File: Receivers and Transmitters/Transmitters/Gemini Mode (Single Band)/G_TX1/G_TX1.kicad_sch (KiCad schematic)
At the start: 15 parts, among them J1 Conn_01x05_Socket, J2 Conn_01x03_Socket, J3 Conn_01x04_Socket, J4 Conn_02x06_Odd_Even, U1 TPS7A4701xRGW, U2 ESP32-WROOM-32, U3 E28-2G4M27S, U5 E28-2G4M27S

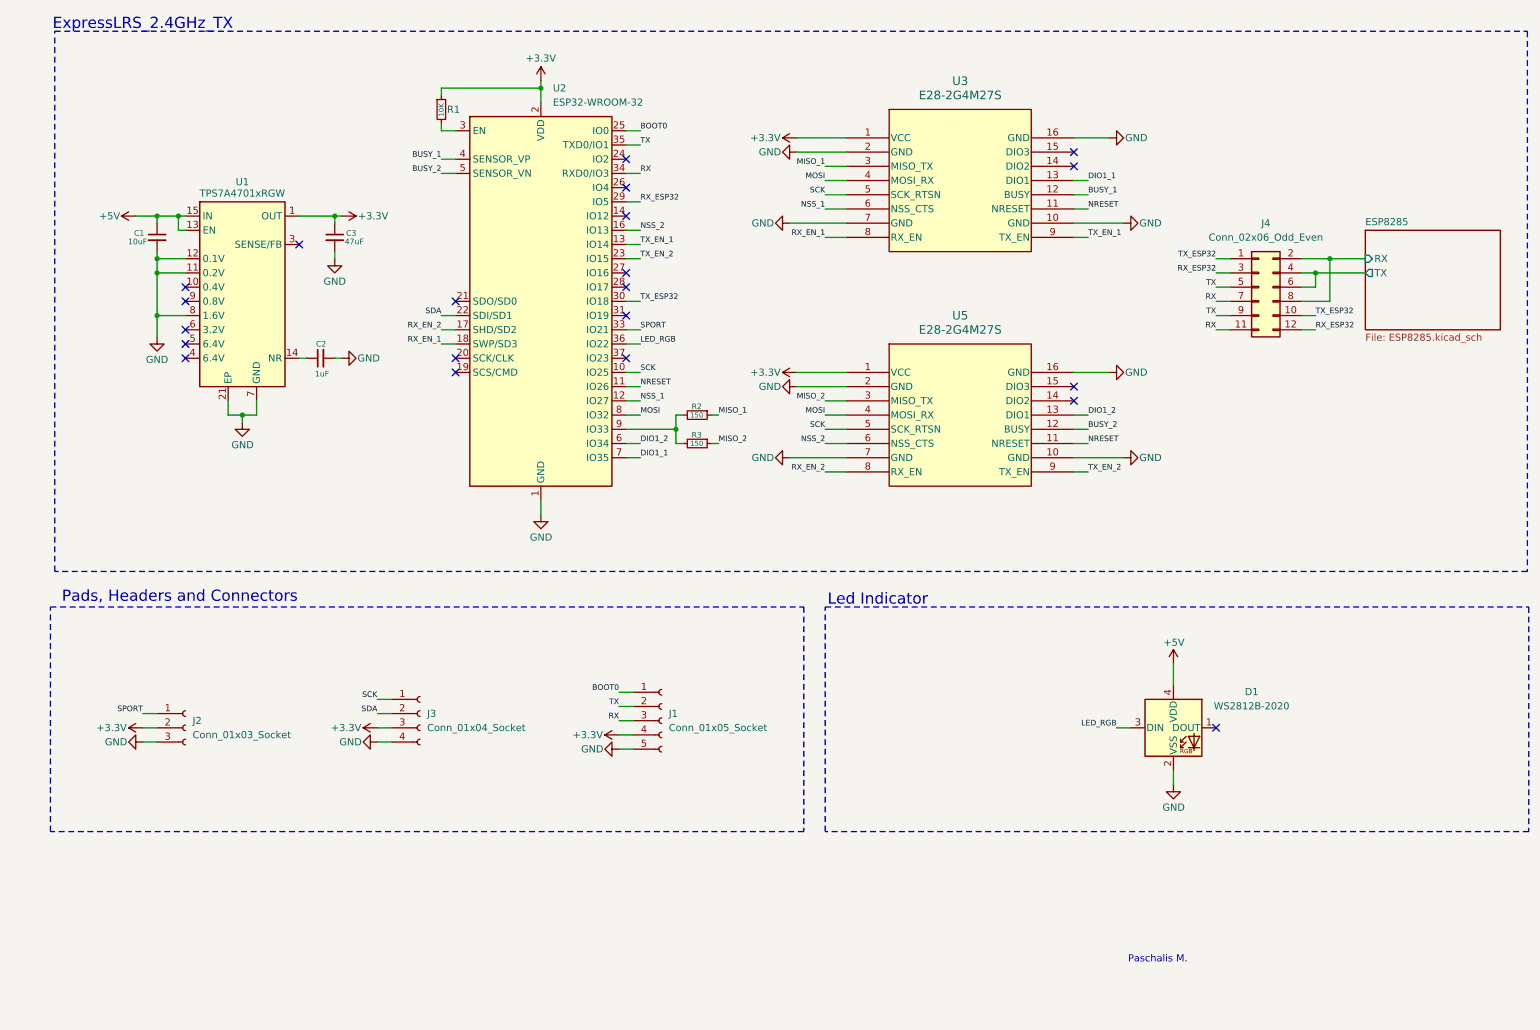
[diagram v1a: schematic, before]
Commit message: Update Antenna Diversity (AD1_2.4G), True Antenna Diversity (TD1_2.4G), and Gemini Mode transmitter (G_TX1): Modify KiCad files, add BOMs and production files; update images, docs, videos, and README; remove outdated Mechanical CAD file
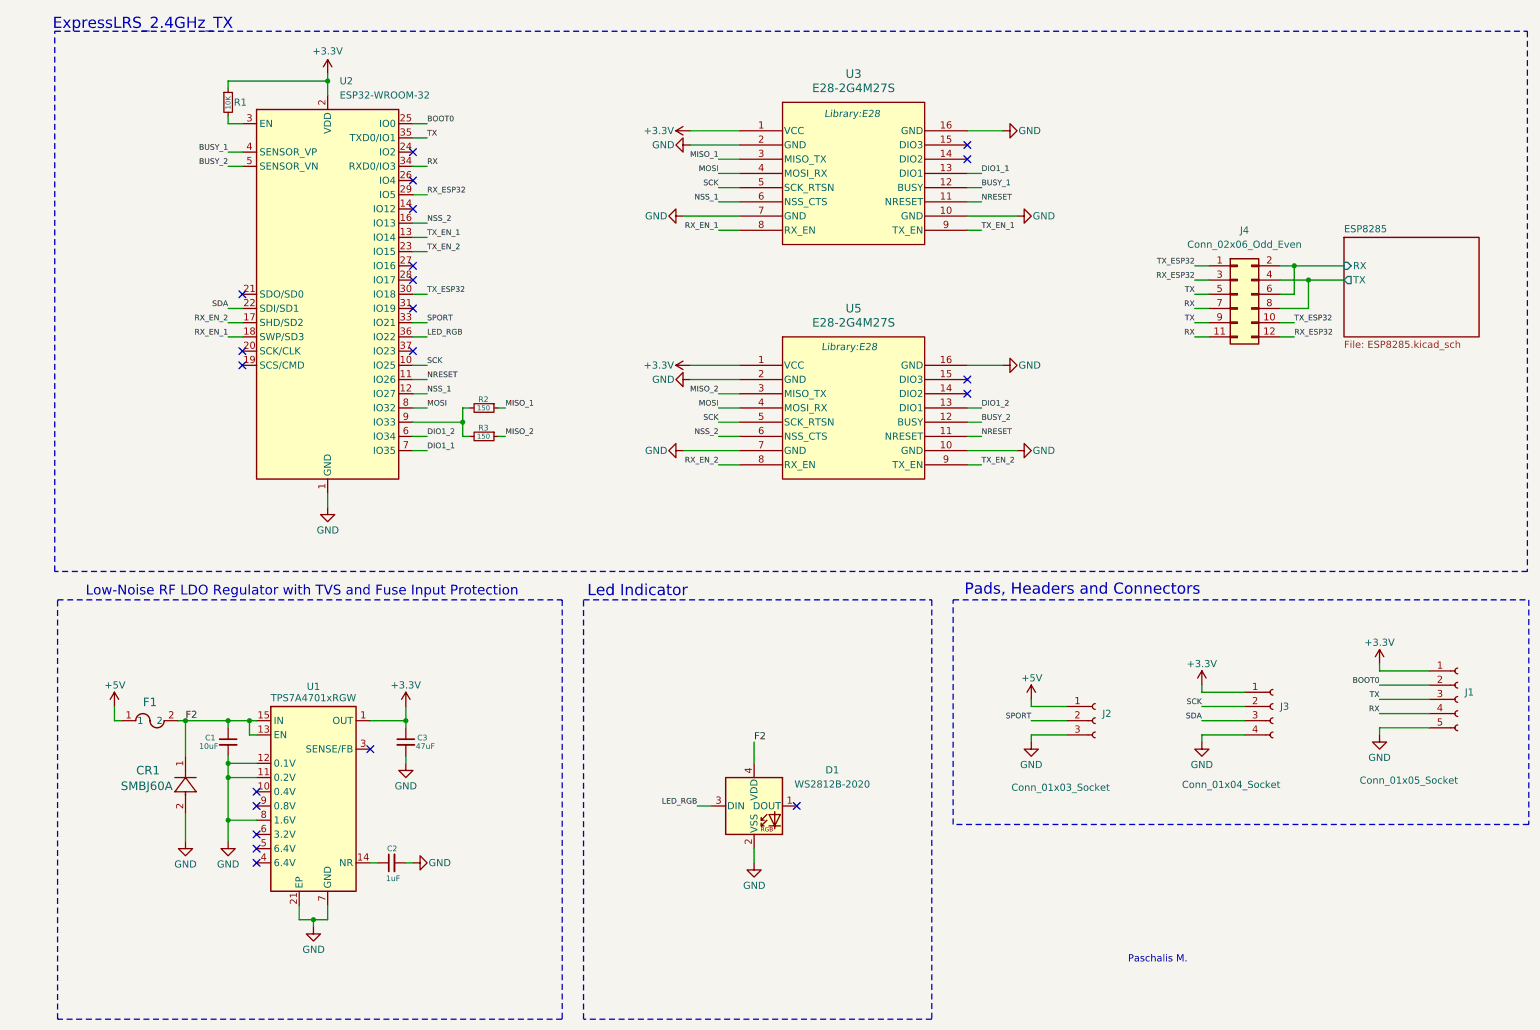
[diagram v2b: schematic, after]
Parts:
- added CR1: SMBJ60A, ul_SMBJ60A:SMBJSeries_LTF, symbol ul_SMBJ60A:SMBJ60A
- added F1: MF-PSMF020X-2, ul_MF-PSMF020X-2:FUSE_F020X_BRN, symbol ul_MF-PSMF020X-2:MF-PSMF020X-2
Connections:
- net +3.3V: now also J1.1 (Pin_1), J3.1 (Pin_1); no longer J1.4 (Pin_4), J2.2 (Pin_2), J3.3 (Pin_3)
- net +5V: now also J2.1 (Pin_1), F1.1; no longer C1.1, D1.4 (VDD), U1.13 (EN), U1.15 (IN), U1.16 (IN)
- net BOOT0: now also J1.2 (Pin_2); no longer J1.1 (Pin_1)
- net ESP8285/RX: now also J4.6 (Pin_6); no longer J4.8 (Pin_8)
- net ESP8285/TX: now also J4.8 (Pin_8); no longer J4.6 (Pin_6)
- net GND: now also CR1.2
- net RX: now also J1.4 (Pin_4); no longer J1.3 (Pin_3)
- net SCK: now also J3.2 (Pin_2); no longer J3.1 (Pin_1)
- net SDA: now also J3.3 (Pin_3); no longer J3.2 (Pin_2)
- net SPORT: now also J2.2 (Pin_2); no longer J2.1 (Pin_1)
- net TX: now also J1.3 (Pin_3); no longer J1.2 (Pin_2)
- new net F2: C1.1, CR1.1, D1.4 (VDD), F1.2, U1.13 (EN), U1.15 (IN), U1.16 (IN)
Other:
- note added: "Low-Noise RF LDO Regulator with TVS and Fuse Input Protection"
- company: https://github.com/Paschalis | TeodoraMiu -> https://github.com/Paschalis
- title: TX3_2.4G -> G_TX1_2.4G
- moved on the sheet: C1, C2, C3, D1, J1, J2, J3, J4, R1, R2, R3, U1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

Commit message: Update G_TX1 Freecad for enclosure and KiCad files (schematics, PCB, and project) - added fan pin headers
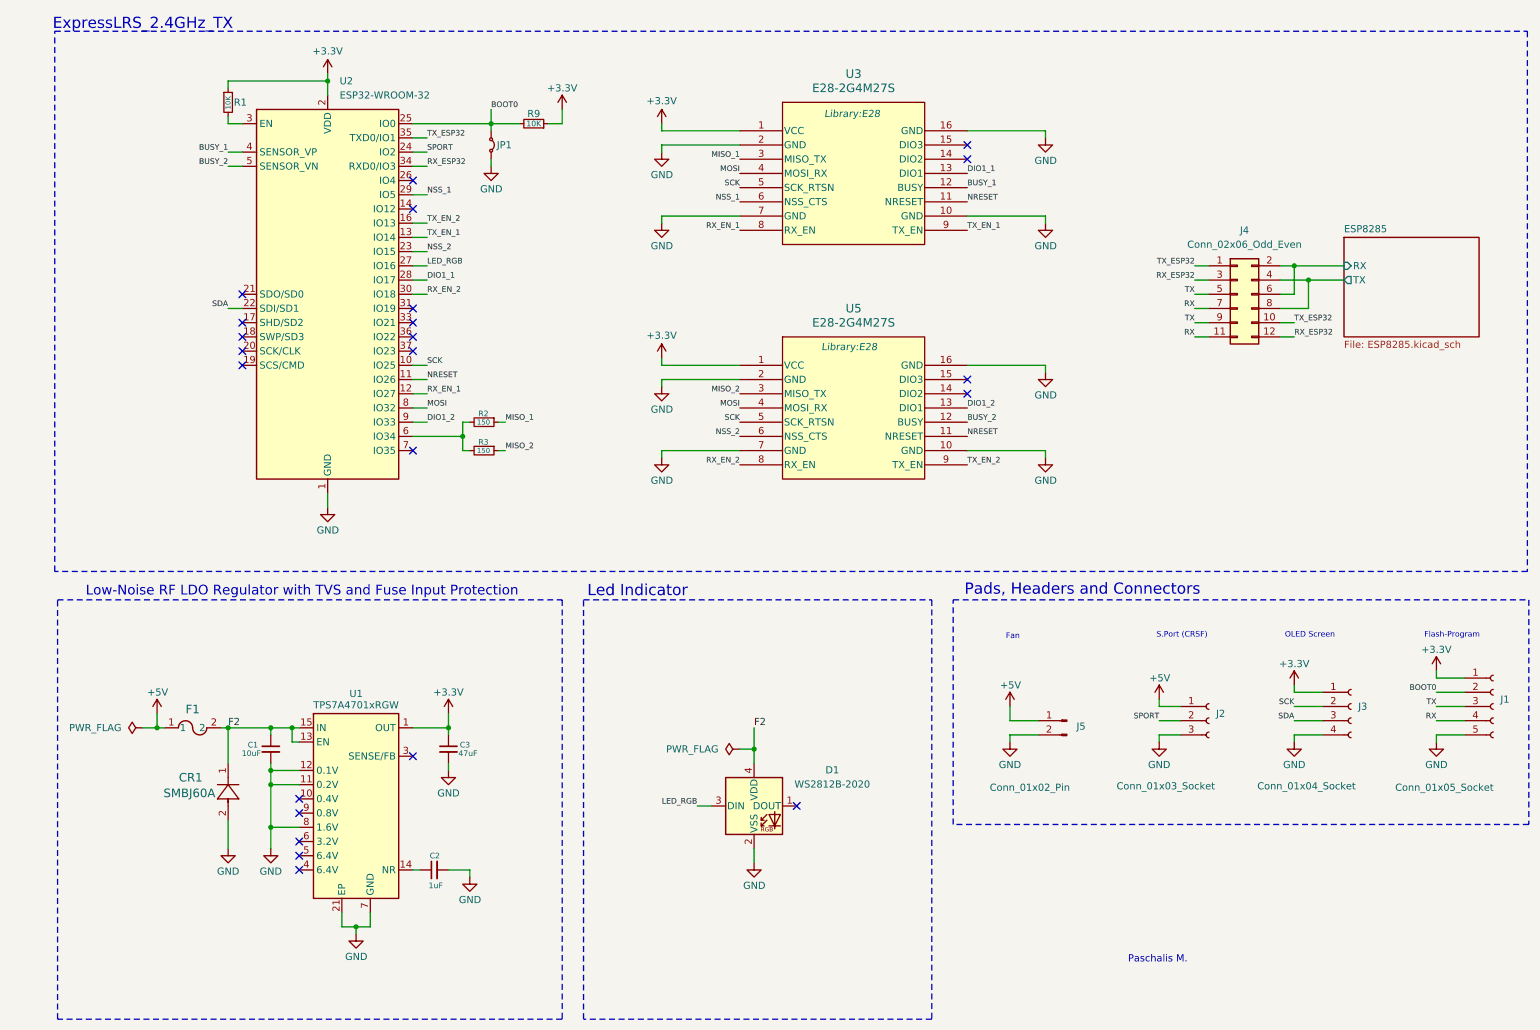
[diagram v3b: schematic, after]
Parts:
- added J5: Conn_01x02_Pin, Connector_PinHeader_2.00mm:PinHeader_1x02_P2.00mm_Vertical, symbol Connector:Conn_01x02_Pin
- added JP1: Jumper_2_Small_Bridged, TestPoint:TestPoint_2Pads_Pitch2.54mm_Drill0.8mm, symbol Jumper:Jumper_2_Small_Bridged
- added R9: 10K, Resistor_SMD:R_0603_1608Metric_Pad0.98x0.95mm_HandSolder, symbol Device:R_Small
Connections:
- net +3.3V: now also R9.1
- net +5V: now also J5.1 (Pin_1)
- net BOOT0: now also JP1.1 (A), R9.2
- net DIO1_1: now also U2.28 (IO17); no longer U2.7 (IO35)
- net DIO1_2: now also U2.9 (IO33); no longer U2.6 (IO34)
- net GND: now also J5.2 (Pin_2), JP1.2 (B)
- net LED_RGB: now also U2.27 (IO16); no longer U2.36 (IO22)
- net NSS_1: now also U2.29 (IO5); no longer U2.12 (IO27)
- net NSS_2: now also U2.23 (IO15); no longer U2.16 (IO13)
- net RX: no longer U2.34 (RXD0/IO3)
- net RX_EN_1: now also U2.12 (IO27); no longer U2.18 (SWP/SD3)
- net RX_EN_2: now also U2.30 (IO18); no longer U2.17 (SHD/SD2)
- net RX_ESP32: now also U2.34 (RXD0/IO3); no longer U2.29 (IO5)
- net SPORT: now also U2.24 (IO2); no longer U2.33 (IO21)
- net TX: no longer U2.35 (TXD0/IO1)
- net TX_EN_2: now also U2.16 (IO13); no longer U2.23 (IO15)
- net TX_ESP32: now also U2.35 (TXD0/IO1); no longer U2.30 (IO18)
- net at R2.2, R3.2: now also U2.6 (IO34); no longer U2.9 (IO33)
- no-connect marks 21 -> 23
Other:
- note added: "Fan"
- note added: "Flash-Program"
- note added: "OLED Screen"
- note added: "S.Port (CRSF)"
- moved on the sheet: C1, C2, C3, CR1, F1, J1, J2, J3, R2, R3, U1
